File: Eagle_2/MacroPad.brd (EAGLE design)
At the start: 100 x 80 mm, 40 parts, among them SW00 SWITCH-SMD-SCHURTER-1241.1612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, SW01 KEYSWITCH-PLAIN-MX-1U, SW02 KEYSWITCH-PLAIN-MX-1U, SW03 KEYSWITCH-PLAIN-MX-1U, SW04 KEYSWITCH-PLAIN-MX-1U, SW05 KEYSWITCH-PLAIN-MX-1U, SW06 KEYSWITCH-PLAIN-MX-1U, SW07 KEYSWITCH-PLAIN-MX-1U, SW08 KEYSWITCH-PLAIN-MX-1U, SW09 KEYSWITCH-PLAIN-MX-1U, SW10 KEYSWITCH-PLAIN-MX-1U, SW11 KEYSWITCH-PLAIN-MX-1U, SW12 KEYSWITCH-PLAIN-MX-1U

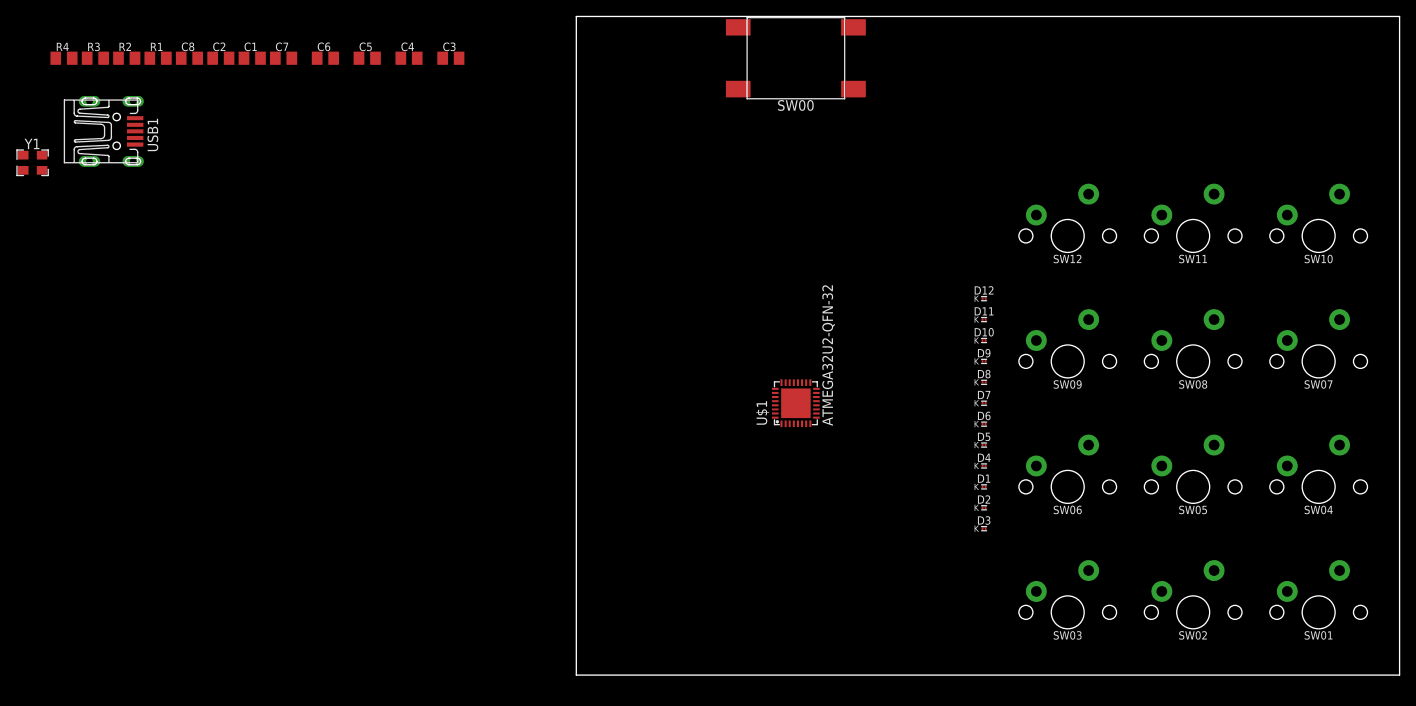
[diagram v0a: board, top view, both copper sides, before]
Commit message: Update switch and chip footprints, and switch array pins
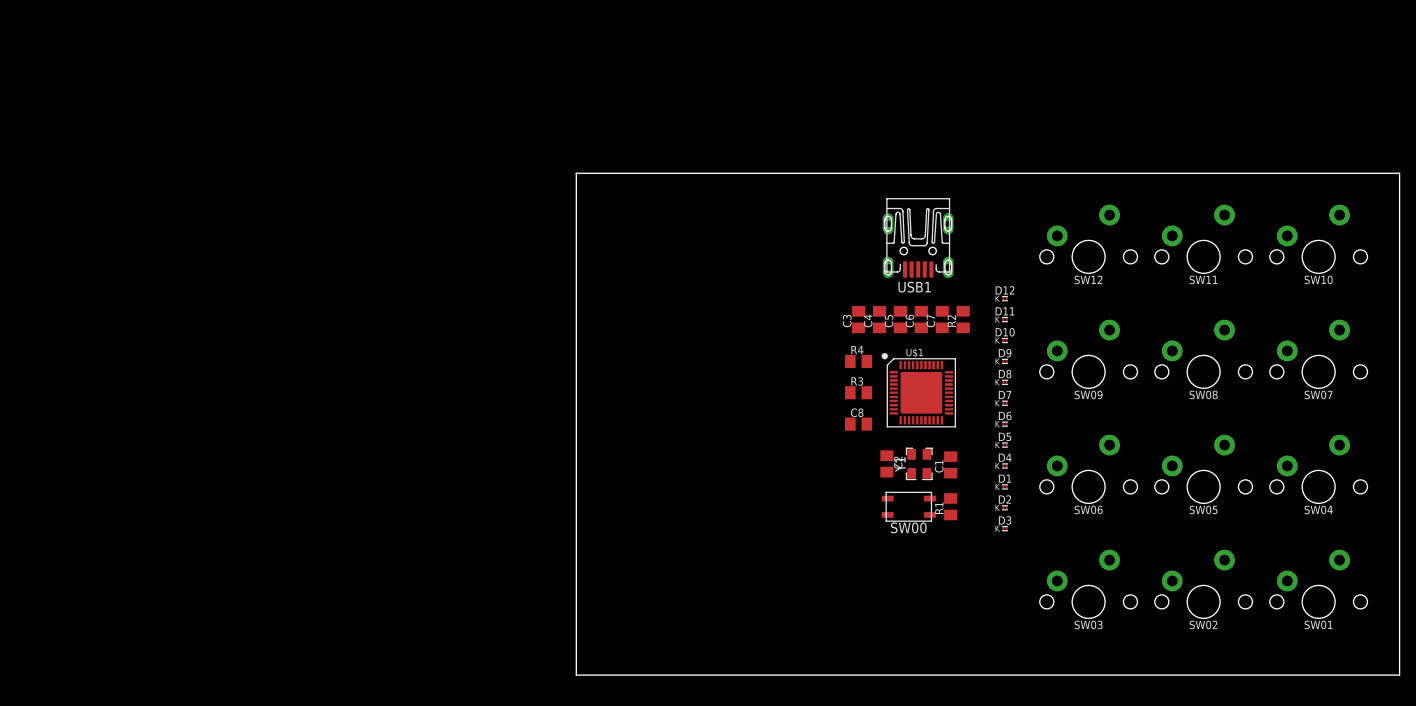
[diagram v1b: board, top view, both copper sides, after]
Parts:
- SW00: value SWITCH-SMD-SCHURTER-1241.1612.11 -> SWITCH-SMD-EVQP-P2602W; device Hardware:SWITCH-SMD-SCHURTER-1241.1612.11 -> Hardware:SWITCH-SMD-EVQP-P2602W
- U$1: value ATMEGA32U2-QFN-32 -> ATMEGA32U4-QFN44; device Controller:QFN-32 -> Controller:QFN-44
- moved Y1 113.7 mm to (41.7, 25.7), turned to 90 degrees
- moved R1 110.6 mm to (45.5, 20.4), turned to 90 degrees
- moved R2 106.4 mm to (47.0, 43.2), turned to 90 degrees
- moved USB1 104.1 mm to (41.5, 57.9), turned to 270 degrees
- moved R4 103.3 mm to (34.3, 38.1)
- moved R3 101.2 mm to (34.3, 34.3)
- moved C1 98.2 mm to (45.5, 25.5), turned to 90 degrees
- moved C2 94.7 mm to (37.7, 25.7), turned to 270 degrees
- moved C8 92.6 mm to (34.3, 30.5)
- moved C7 86.1 mm to (44.5, 43.2), turned to 90 degrees
- moved C6 79.0 mm to (41.9, 43.2), turned to 90 degrees
- moved C5 72.1 mm to (39.4, 43.2), turned to 90 degrees
- moved C4 65.4 mm to (36.8, 43.2), turned to 90 degrees
- moved C3 58.8 mm to (34.3, 43.2), turned to 90 degrees
- moved SW00 56.2 mm to (40.4, 20.4)
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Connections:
- net GND: now also R2.2, U$1.15, U$1.23, U$1.35, U$1.43, U$1.5, U$1.TAB; no longer U$1.28, U$1.3, U$1.PAD
- net N$1: now also U$1.16; no longer U$1.2
- net N$10: now also U$1.31; no longer U$1.12
- net N$14: now also U$1.25; no longer U$1.9
- net N$16: now also U$1.29; no longer U$1.10
- net N$2: now also U$1.17; no longer U$1.1
- net N$26: now also U$1.26; no longer U$1.8
- net N$3: now also U$1.13; no longer U$1.24
- net N$32: now also U$1.27; no longer U$1.7
- net N$38: now also U$1.28; no longer U$1.6
- net N$4: now also U$1.33; no longer U$1.13
- net N$40: now also U$1.30; no longer U$1.11
- net N$6: now also U$1.3; no longer U$1.29
- net N$8: now also U$1.4; no longer U$1.30
- net UCAP: now also U$1.6; no longer U$1.27
- net UGND: no longer R2.2
- net VCC: now also U$1.14, U$1.2, U$1.24, U$1.34, U$1.44, U$1.7; no longer U$1.31, U$1.32, U$1.4
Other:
- board size 100 x 80 mm -> 100 x 61 mm

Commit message: Route rows
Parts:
- moved D10 19.1 mm to (53.3, 59.7)
- moved D11 15.3 mm to (53.3, 58.4)
- moved D7 12.8 mm to (53.3, 45.7)
- moved D12 11.5 mm to (53.3, 57.1)
- moved D8 8.98 mm to (53.3, 44.5)
- moved D4 6.48 mm to (53.3, 31.8)
- moved D1 5.24 mm to (53.3, 17.8)
- moved D9 5.24 mm to (53.3, 43.2)
- moved D2 4.02 mm to (53.3, 16.5)
- moved D3 2.84 mm to (53.3, 15.2)
- moved D5 2.84 mm to (53.3, 30.5)
- moved D6 1.80 mm to (53.3, 29.2)
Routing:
- net N$9: track 0.00 -> 40.8 mm
- net N$27: track 0.00 -> 40.8 mm
- net N$36: track 0.00 -> 40.8 mm
- net N$18: track 0.00 -> 40.8 mm
- net N$38: track 0.00 -> 32.2 mm
- net N$30: track 0.00 -> 26.3 mm
- net N$39: track 0.00 -> 26.3 mm
- net N$21: track 0.00 -> 26.3 mm
- net N$12: track 0.00 -> 26.3 mm
- net N$14: track 0.00 -> 24.4 mm
- net N$32: track 0.00 -> 18.9 mm
- net N$33: track 0.00 -> 11.8 mm
- net N$24: track 0.00 -> 11.8 mm
- net N$15: track 0.00 -> 11.8 mm
- net N$42: track 0.00 -> 11.8 mm
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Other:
- board size 100 x 61 mm -> 100 x 62.2 mm

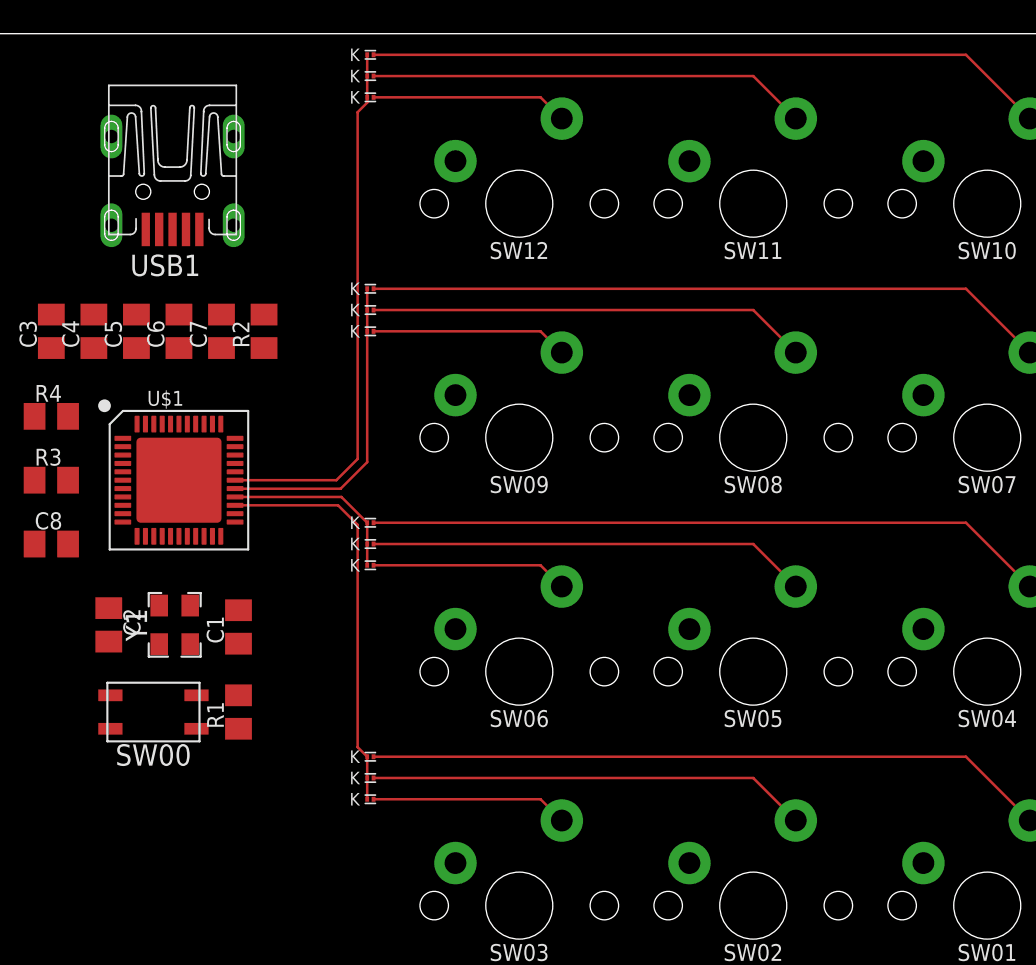
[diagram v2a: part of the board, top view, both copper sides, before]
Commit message: Route columns
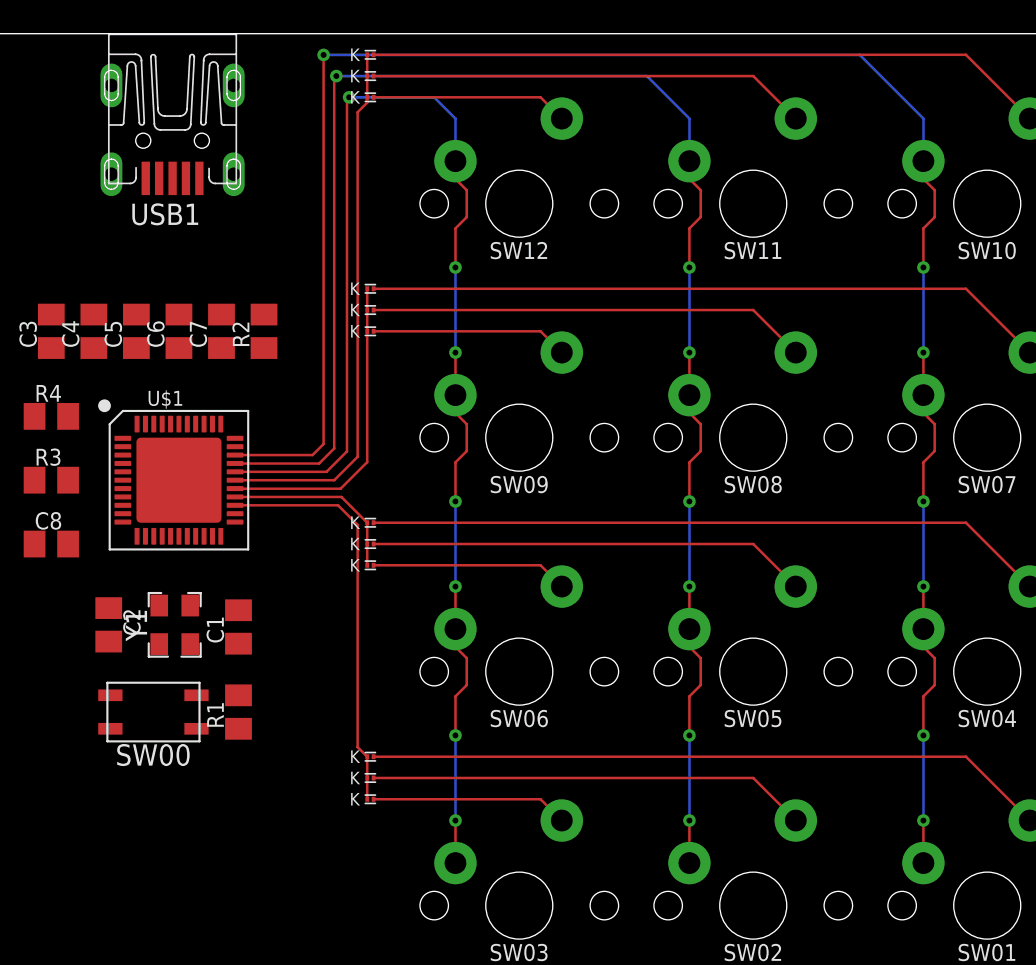
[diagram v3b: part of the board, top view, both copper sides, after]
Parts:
- moved USB1 3.05 mm to (41.5, 61.0)
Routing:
- net N$10: track 0.00 -> 112.3 mm, vias 0 -> 7
- net N$40: track 0.00 -> 96.8 mm, vias 0 -> 7
- net N$16: track 0.00 -> 80.2 mm, vias 0 -> 7

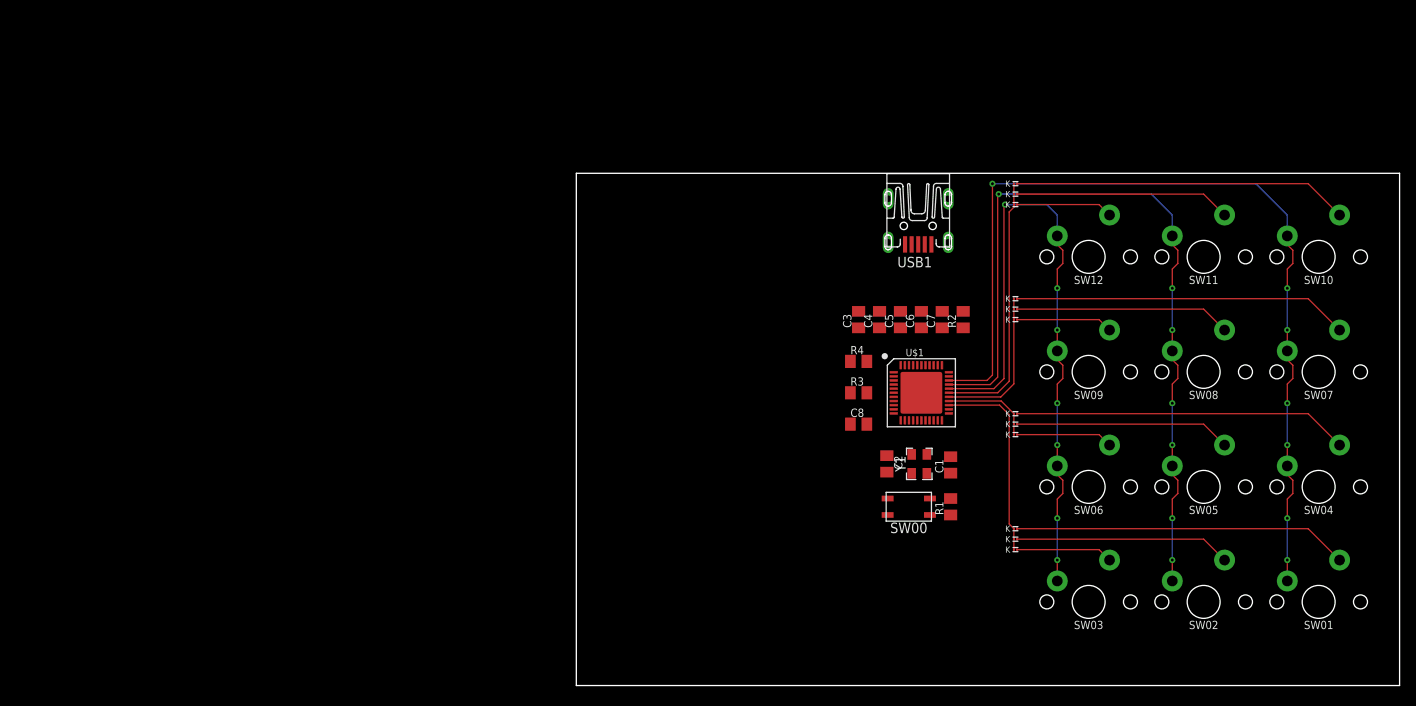
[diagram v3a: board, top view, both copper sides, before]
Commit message: Routed board
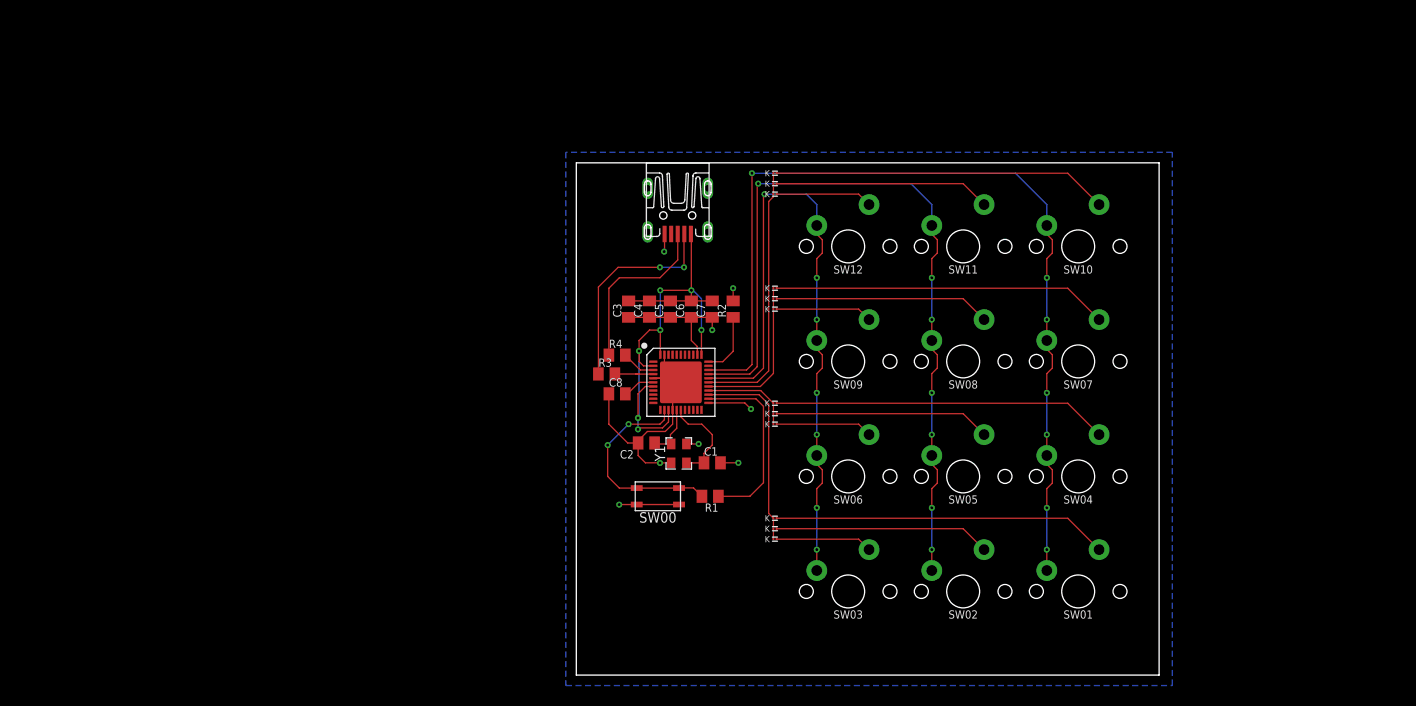
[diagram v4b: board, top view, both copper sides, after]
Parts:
- moved R3 30.7 mm to (3.68, 36.6)
- moved SW00 30.5 mm to (9.91, 21.7)
- moved C8 29.6 mm to (4.95, 34.2)
- moved R4 29.3 mm to (4.95, 38.9)
- moved C2 29.3 mm to (8.51, 28.2), turned to 180 degrees
- moved D1 29.2 mm to (24.1, 19.1)
- moved D10 29.2 mm to (24.1, 61.0)
- moved D11 29.2 mm to (24.1, 59.7)
- moved D12 29.2 mm to (24.1, 58.4)
- moved D2 29.2 mm to (24.1, 17.8)
- moved D3 29.2 mm to (24.1, 16.5)
- moved D4 29.2 mm to (24.1, 33.0)
- moved D5 29.2 mm to (24.1, 31.8)
- moved D6 29.2 mm to (24.1, 30.5)
- moved D7 29.2 mm to (24.1, 47.0)
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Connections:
- removed net GND: C8.1, R2.2, U$1.15, U$1.23, U$1.35, U$1.43, U$1.5, U$1.TAB, USB1.GND, USB1.SHIELD@1, USB1.SHIELD@2, USB1.SHIELD@3, USB1.SHIELD@4
- net UGND: now also C8.1, R2.2, U$1.15, U$1.23, U$1.35, U$1.43, U$1.5, U$1.TAB, USB1.GND, USB1.SHIELD@1, USB1.SHIELD@2, USB1.SHIELD@3, USB1.SHIELD@4
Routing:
- net VCC: track 0.00 -> 88.5 mm, vias 0 -> 7
- net UGND: track 0.00 -> 70.8 mm, vias 0 -> 8
- net N$7: track 0.00 -> 26.0 mm, vias 0 -> 2
- net N$3: track 0.00 -> 25.6 mm, vias 0 -> 2
- net N$5: track 0.00 -> 21.1 mm
- net N$2: track 0.00 -> 11.5 mm
- net N$4: track 0.00 -> 7.65 mm
- net N$1: track 0.00 -> 6.55 mm
- net N$8: track 0.00 -> 5.07 mm
- net N$6: track 0.00 -> 4.14 mm
- net UCAP: track 0.00 -> 3.98 mm
- added copper zone on layer 16, net UGND
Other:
- board size 100 x 62.2 mm -> 70.8 x 62.2 mm

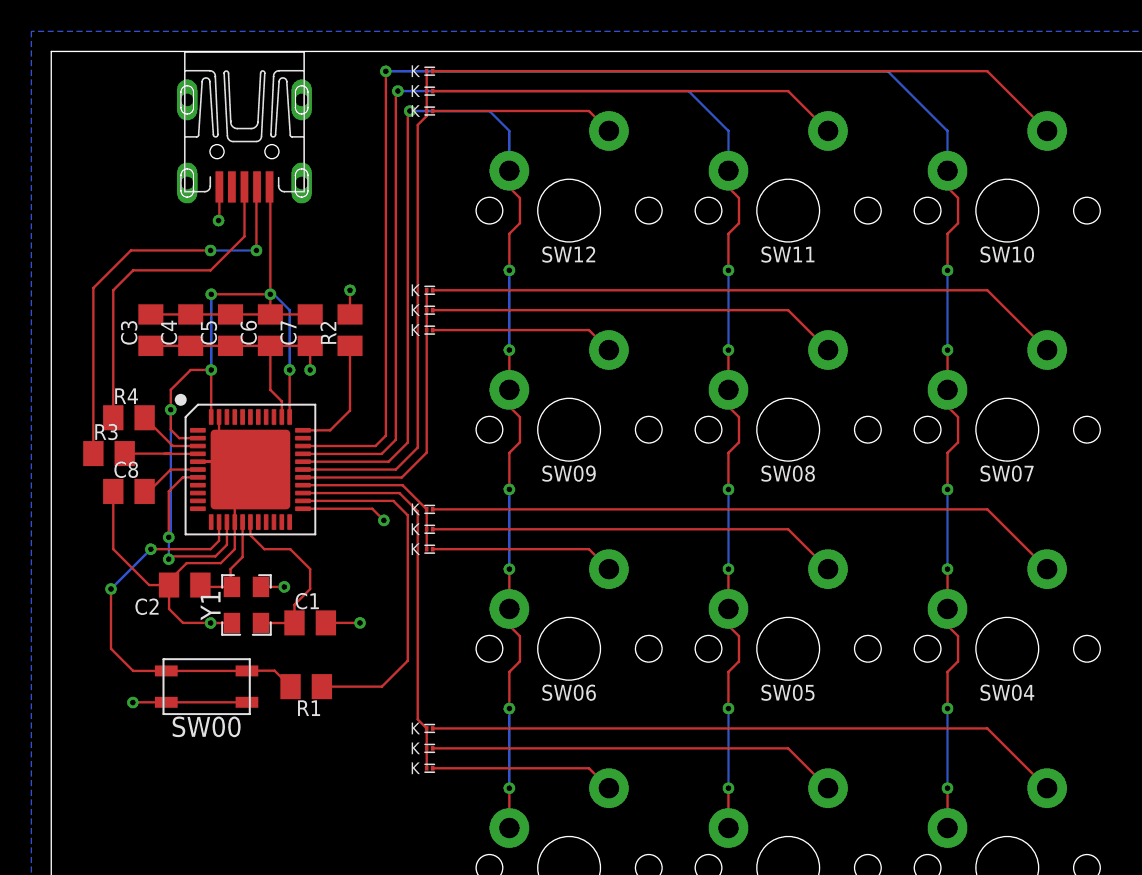
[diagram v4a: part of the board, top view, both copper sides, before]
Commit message: Compress row traces
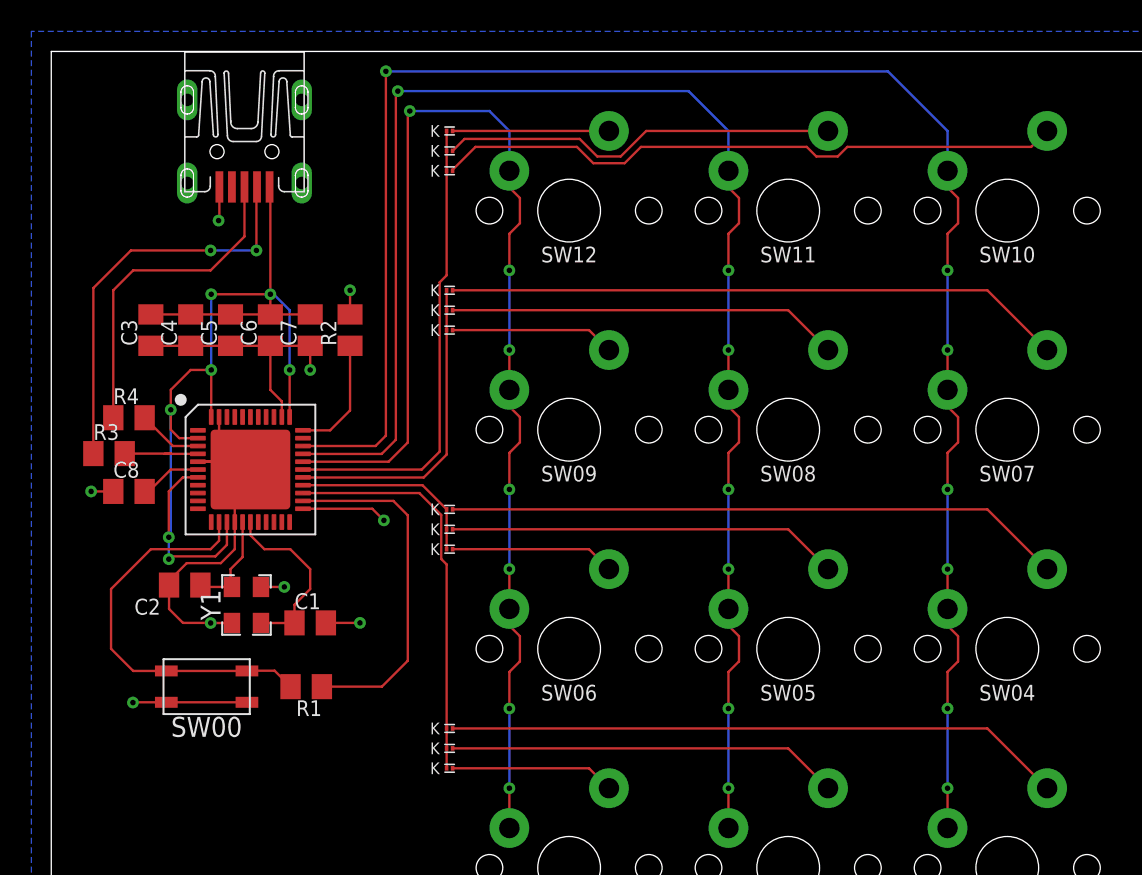
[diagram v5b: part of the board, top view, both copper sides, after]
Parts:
- moved D10 6.48 mm to (25.4, 54.6)
- moved D11 4.02 mm to (25.4, 55.9)
- moved D12 1.80 mm to (25.4, 57.1)
- moved D1 1.27 mm to (25.4, 19.1)
- moved D2 1.27 mm to (25.4, 17.8)
- moved D3 1.27 mm to (25.4, 16.5)
- moved D4 1.27 mm to (25.4, 33.0)
- moved D5 1.27 mm to (25.4, 31.8)
- moved D6 1.27 mm to (25.4, 30.5)
- moved D7 1.27 mm to (25.4, 47.0)
- moved D8 1.27 mm to (25.4, 45.7)
- moved D9 1.27 mm to (25.4, 44.5)
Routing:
- net UGND: track 70.8 -> 64.0 mm, vias 8 -> 9
- net N$38: track 32.1 -> 29.8 mm
- net N$42: track 11.8 -> 9.97 mm
- net N$32: track 18.9 -> 20.2 mm
- net N$9: track 40.8 -> 39.5 mm
- net N$27: track 40.8 -> 39.5 mm
- net N$18: track 40.8 -> 39.5 mm
- net N$33: track 11.8 -> 10.5 mm
- net N$30: track 26.3 -> 25.0 mm
- net N$26: track 11.1 -> 12.3 mm
- net N$24: track 11.8 -> 10.5 mm
- net N$21: track 26.3 -> 25.0 mm
- net N$15: track 11.8 -> 10.5 mm
- net N$14: track 24.4 -> 25.7 mm
- net N$12: track 26.3 -> 25.0 mm
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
